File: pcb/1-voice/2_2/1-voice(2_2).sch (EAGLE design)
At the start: 74 parts, among them U1 THAT2180

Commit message: Finish 1-voice brd, start making it work
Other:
- note added: "- Add Power LEDs"
- note added: "- Add Power Switch"
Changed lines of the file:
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@@
 <text x="40.64" y="25.4" size="1.778" layer="97">VDD
 VSS</text>
+<text x="109.22" y="25.4" size="1.778" layer="90">- Add Power Switch</text>
+<text x="109.22" y="22.86" size="1.778" layer="90">- Add Power LEDs</text>
 </plain>
 <instances>

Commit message: Made v2
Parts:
- removed TP1: TPB1,27, testpad:TPB1,27
- added C26: 0.1u, rcl:C-EUC0603
- added LED1, LED2, LED3, LED4: (no value), led:LEDSMT1206
- added R14: 5.1k, rcl:R-US_R0603
- added R15: 20k, rcl:R-US_R0603
- added R16: 330k, rcl:R-US_R0603
- added R17, R18: 4.7k, rcl:R-US_R0603
- added R19, R20, R21, R22: 1k, rcl:R-US_R0603
- added SJ1: (no value), jumper:SJ
- added U$5: TL072, synth:TL072
- added U$6: SWITCH-DPDT, synth:SWITCH-DPDT
- C25: value 10u -> 0.1u
- R10: value 4.7k -> 20k
- R13: value 330 -> 330k
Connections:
- new net -15V-IN: JP7.1, U$6.P$5
- new net 15V-IN: JP7.3, U$6.P$2
- new net LED: LED4.A, U$2.PA15
- new net N$16: R14.2, U1.V-
- new net N$17: LED1.C, R19.2
- new net N$18: LED2.C, R20.2
- new net N$19: R16.1, R17.2, R18.1
- new net N$20: R15.1, R16.2, U$5G$2.IN+
- new net N$21: LED3.A, R21.2
- new net N$22: LED4.C, R22.2
- net +15V: now also C25.2, LED1.A, U$5G$3.V+, U$6.P$1; no longer JP7.3
- net +3V3: now also LED2.A, R18.2
- net -15V: now also C26.1, LED3.C, R14.1, U$5G$3.V-, U$6.P$4; no longer JP7.1, U1.V-
- net F-CTRL0: now also R13.2; no longer C25.1
- net F-CTRL0-EXP: now also SJ1.1; no longer Q2A.C
- net GND: now also C25.1, C26.2, R15.2, R17.1, R19.1, R20.1, R21.1, R22.1; no longer R13.1
- net N$1: now also R10.2, R13.1, U$5G$2.IN-; no longer C25.2, R10.1
- net N$15: now also R10.1, U$5G$2.OUT; no longer R10.2, R13.2
- net N$7: now also Q2A.C, SJ1.2; no longer TP1.TP, U$2.VBAT
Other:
- note removed: "- Add Power LEDs"
- note removed: "- Add Power Switch"
- moved on the sheet: C21, C22, C23, C24, C25, R10, R11, R12, R13, TP3, TP7, TP8

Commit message: Add LED blink code, Update schem with LED R values
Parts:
- R19: value 1k -> 100k
- R21: value 1k -> 10k
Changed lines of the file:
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@@
 <?xml version="1.0" encoding="utf-8"?>
 <!DOCTYPE eagle SYSTEM "eagle.dtd">
-<eagle version="9.2.1">
+<eagle version="9.3.2">
 <drawing>
 <settings>
@@
 <part name="LED3" library="led" library_urn="urn:adsk.eagle:library:259" deviceset="LED" device="SMT1206" package3d_urn="urn:adsk.eagle:package:15796/2"/>
 <part name="P+10" library="supply1" library_urn="urn:adsk.eagle:library:371" deviceset="+15V" device=""/>
-<part name="R19" library="rcl" library_urn="urn:adsk.eagle:library:334" deviceset="R-US_" device="R0603" package3d_urn="urn:adsk.eagle:package:23555/3" value="1k"/>
+<part name="R19" library="rcl" library_urn="urn:adsk.eagle:library:334" deviceset="R-US_" device="R0603" package3d_urn="urn:adsk.eagle:package:23555/3" value="100k"/>
 <part name="GND23" library="supply1" library_urn="urn:adsk.eagle:library:371" deviceset="GND" device=""/>
 <part name="+3V10" library="supply1" library_urn="urn:adsk.eagle:library:371" deviceset="+3V3" device=""/>
@@
 <part name="GND24" library="supply1" library_urn="urn:adsk.eagle:library:371" deviceset="GND" device=""/>
 <part name="P-8" library="supply1" library_urn="urn:adsk.eagle:library:371" deviceset="-15V" device=""/>
-<part name="R21" library="rcl" library_urn="urn:adsk.eagle:library:334" deviceset="R-US_" device="R0603" package3d_urn="urn:adsk.eagle:package:23555/3" value="1k"/>
+<part name="R21" library="rcl" library_urn="urn:adsk.eagle:library:334" deviceset="R-US_" device="R0603" package3d_urn="urn:adsk.eagle:package:23555/3" value="10k"/>
 <part name="GND25" library="supply1" library_urn="urn:adsk.eagle:library:371" deviceset="GND" device=""/>
 <part name="LED4" library="led" library_urn="urn:adsk.eagle:library:259" deviceset="LED" device="SMT1206" package3d_urn="urn:adsk.eagle:package:15796/2"/>

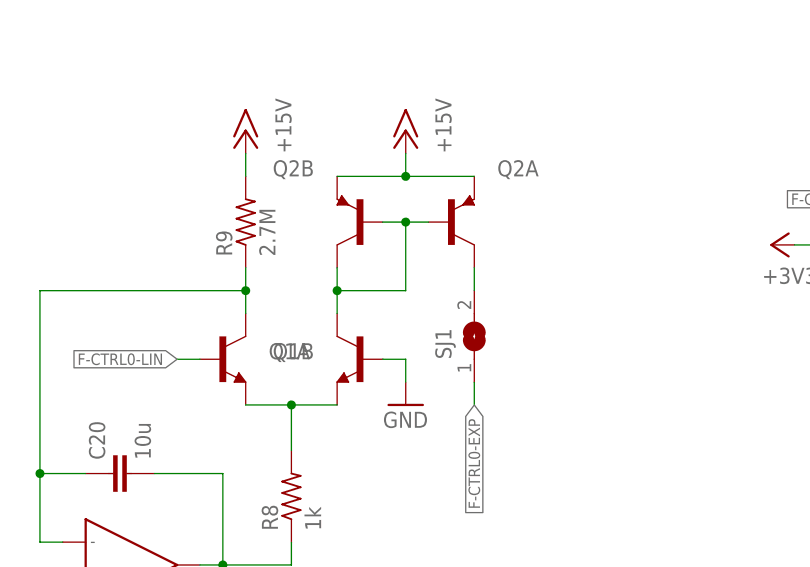
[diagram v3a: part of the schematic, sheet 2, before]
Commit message: Found error in sch values around lin->exp converter
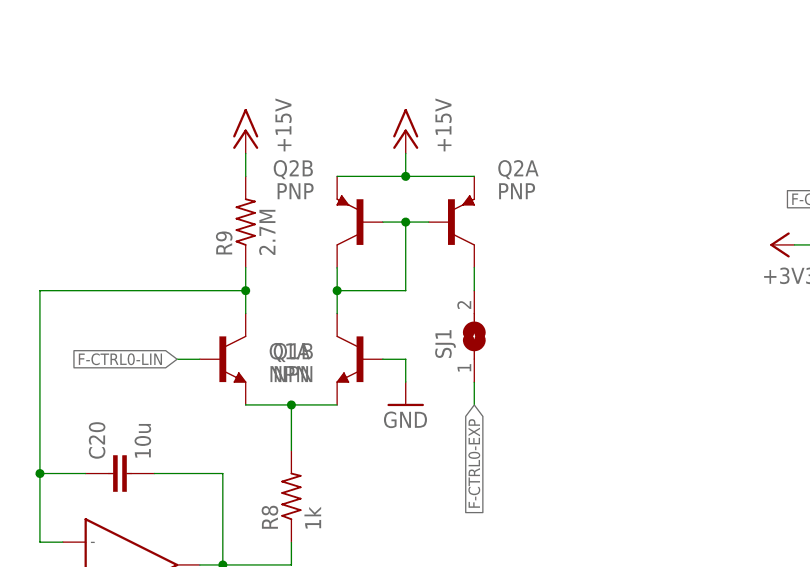
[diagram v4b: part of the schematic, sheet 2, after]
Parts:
- Q1: value (none) -> NPN
- Q2: value (none) -> PNP
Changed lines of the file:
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@@
 <part name="C19" library="rcl" library_urn="urn:adsk.eagle:library:334" deviceset="C-EU" device="C0603" package3d_urn="urn:adsk.eagle:package:23616/2" value="0.1u"/>
 <part name="GND15" library="supply1" library_urn="urn:adsk.eagle:library:371" deviceset="GND" device=""/>
-<part name="Q1" library="LITTLEBITS" deviceset="TRANS-BJT_NPN-DUAL" device="-BC847BS-JBLMASK"/>
-<part name="Q2" library="LITTLEBITS" deviceset="TRANS-BJT_PNP-DUAL" device="-BC857-JBLMASK"/>
+<part name="Q1" library="LITTLEBITS" deviceset="TRANS-BJT_NPN-DUAL" device="-BC847BS-JBLMASK" value="NPN"/>
+<part name="Q2" library="LITTLEBITS" deviceset="TRANS-BJT_PNP-DUAL" device="-BC857-JBLMASK" value="PNP"/>
 <part name="R8" library="rcl" library_urn="urn:adsk.eagle:library:334" deviceset="R-US_" device="R0603" package3d_urn="urn:adsk.eagle:package:23555/3" value="1k"/>
 <part name="C20" library="rcl" library_urn="urn:adsk.eagle:library:334" deviceset="C-EU" device="C0603" package3d_urn="urn:adsk.eagle:package:23616/2" value="10u"/>
